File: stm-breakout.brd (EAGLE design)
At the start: 68 x 68 mm, 5 parts, among them IC1 STM32H757IIT6

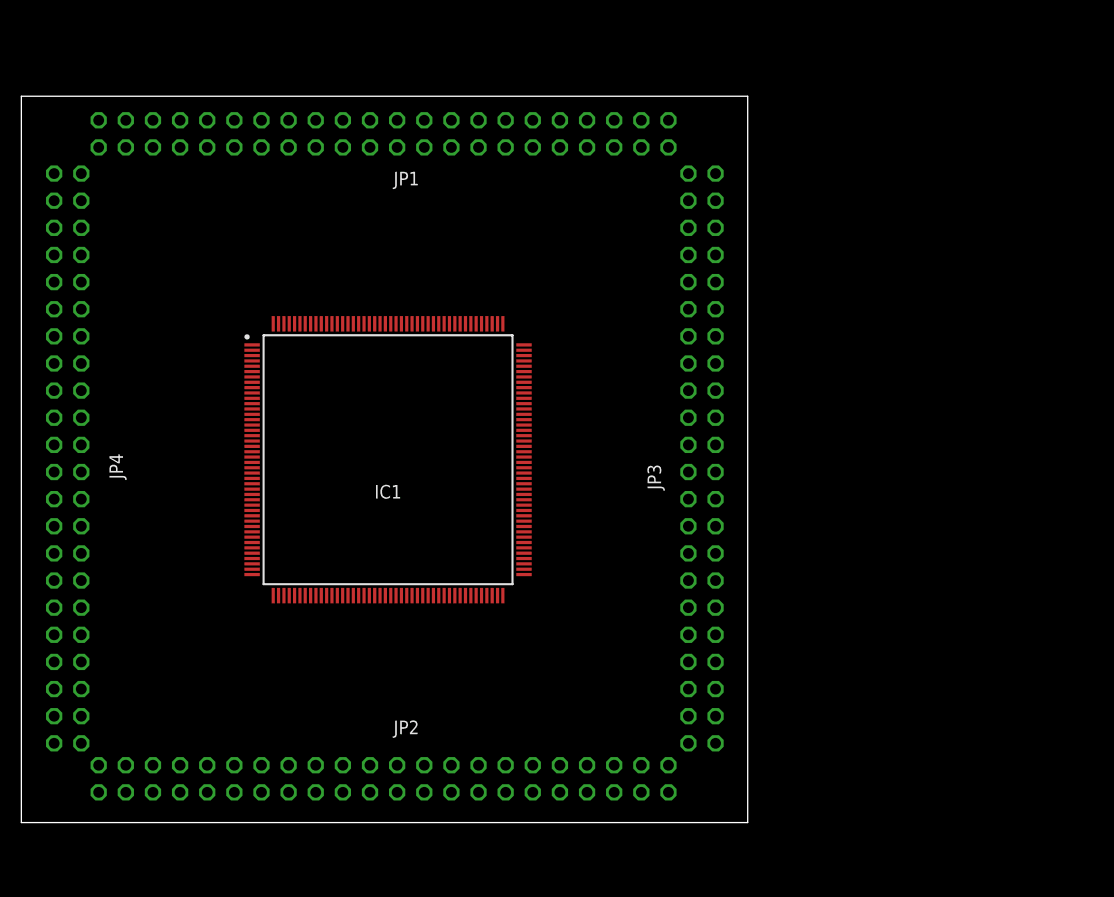
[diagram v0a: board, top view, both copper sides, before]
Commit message: Add in power filtering and SMPS functionality
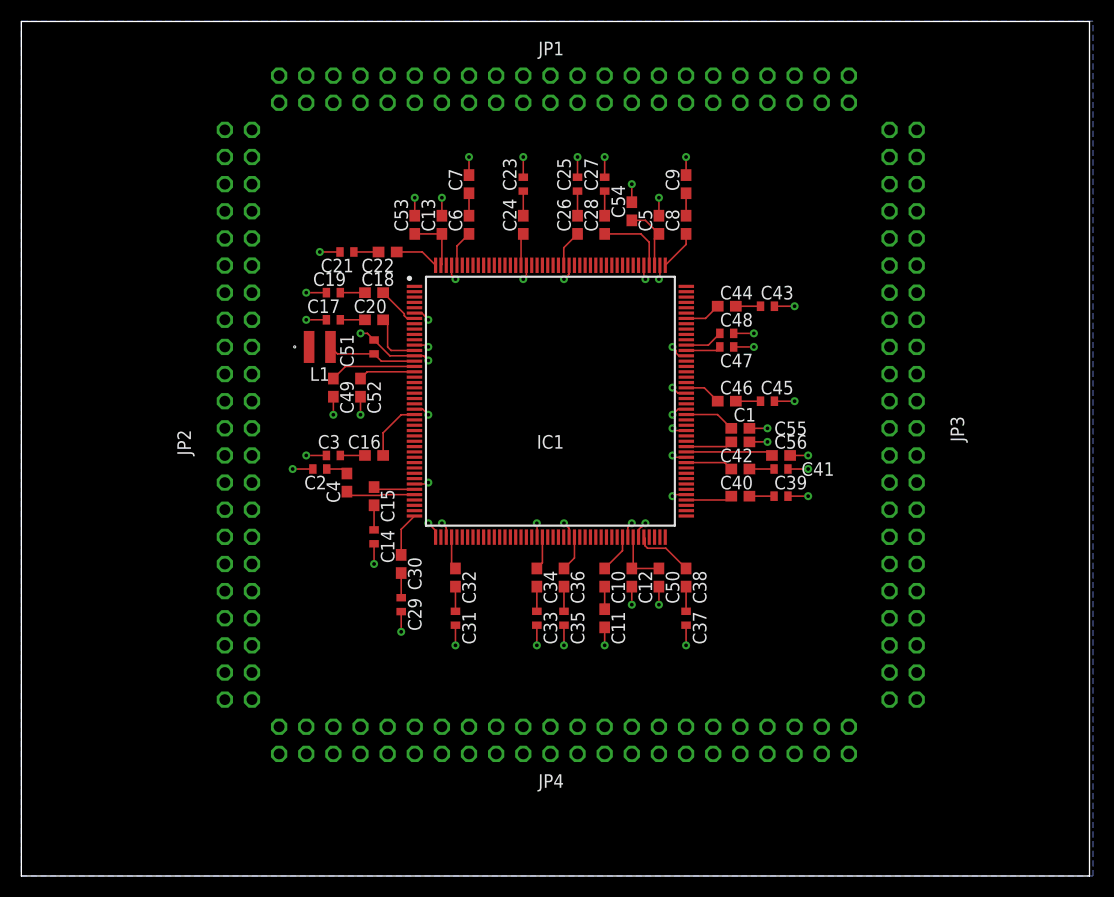
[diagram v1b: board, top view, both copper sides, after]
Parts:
- added C1, C10, C11, C55, C56, C6, C7, C8, C9: 2.2u, rcl:C0603
- added C12, C13, C16, C18, C20, C22, C24, C26, C28, C30, C32, C34, C36, C38, C40, C42, C44, C46, C49, C5: 4.7u, rcl:C0603
- added C14, C17, C19, C2, C21, C23, C25, C27, C29, C3, C31, C33, C35, C37, C39, C41, C43, C45, C47, C48: 100n, rcl:C0402
- added C15, C4: 1u, rcl:C0603
- added C50, C52, C53, C54: 10u, rcl:C0603
- added C51: 220p, rcl:C0402
- added L1: VLS3015CX-2R2M-H, SamacSys_Parts:VLS3015
- moved JP4 51.7 mm to (49.5, 12.7), turned to 180 degrees
- moved JP2 36.0 mm to (20.3, 41.9), turned to 90 degrees
- moved JP3 19.3 mm to (82.5, 41.9)
- moved IC1 16.2 mm to (49.5, 44.5)
- moved JP1 14.9 mm to (49.5, 73.7), turned to 180 degrees
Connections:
- new net GND: C1.2, C11.2, C12.2, C13.2, C14.2, C17.2, C19.2, C2.2, C21.2, C23.2, C25.2, C27.2, C29.2, C3.2, C31.2, C33.2, C35.2, C37.2, C39.2, C41.2, C43.2, C45.2, C47.2, C48.2, C49.2, C5.2, C50.2, C51.2, C52.2, C53.2, C54.2, C55.2, C56.2, C7.2, C9.2, IC1.100, IC1.105, IC1.109, IC1.112, IC1.119, IC1.12, IC1.134, IC1.137, IC1.14, IC1.151, IC1.159, IC1.173, IC1.24, IC1.38, IC1.45, IC1.47, IC1.6, IC1.64, IC1.70, IC1.81, IC1.83, IC1.93
- new net N$1: C2.1, C4.2
- new net N$2: C6.2, C7.1
- new net N$3: C8.2, C9.1
- new net N$4: C10.2, C11.1
- new net VCAPDSI: C1.1, C55.1, C56.1, IC1.101, IC1.102, IC1.108
- new net VDD: C10.1, C12.1, C13.1, C16.1, C18.1, C20.1, C22.1, C24.1, C26.1, C28.1, C30.1, C32.1, C34.1, C36.1, C38.1, C4.1, C40.1, C42.1, C44.1, C46.1, C5.1, C50.1, C52.1, C53.1, C54.1, C6.1, C8.1, IC1.113, IC1.126, IC1.13, IC1.133, IC1.135, IC1.136, IC1.152, IC1.160, IC1.17, IC1.172, IC1.175, IC1.176, IC1.25, IC1.40, IC1.44, IC1.48, IC1.65, IC1.7, IC1.71, IC1.80, IC1.82, IC1.84, IC1.92, IC1.99, L1.1
- new net VDD33USB: C48.1, IC1.121
- new net VDD50USB: C47.1, IC1.120
- new net VIN: C49.1, IC1.16
- new net VLXSMPS: C51.1, IC1.15, L1.2
- new net VREF: C15.1, IC1.39
- new net VREFNF: C14.1, C15.2
- new net VREFNF1: C16.2, C3.1
- new net VREFNF10: C33.1, C34.2
- new net VREFNF11: C35.1, C36.2
- new net VREFNF12: C37.1, C38.2
- new net VREFNF13: C39.1, C40.2
- new net VREFNF14: C41.1, C42.2
- new net VREFNF15: C43.1, C44.2
- new net VREFNF16: C45.1, C46.2
- new net VREFNF2: C17.1, C18.2
- new net VREFNF3: C19.1, C20.2
- new net VREFNF4: C21.1, C22.2
- new net VREFNF5: C23.1, C24.2
- new net VREFNF6: C25.1, C26.2
- new net VREFNF7: C27.1, C28.2
- new net VREFNF8: C29.1, C30.2
- new net VREFNF9: C31.1, C32.2
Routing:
- net VDD: track 0.00 -> 107.1 mm
- net GND: track 0.00 -> 99.5 mm, vias 0 -> 57
- net VCAPDSI: track 0.00 -> 17.3 mm
- net VLXSMPS: track 0.00 -> 8.42 mm
- net VIN: track 0.00 -> 8.06 mm
- net VREF: track 0.00 -> 3.87 mm
- net VDD33USB: track 0.00 -> 3.60 mm
- net VDD50USB: track 0.00 -> 3.27 mm
- net VREFNF7: track 0.00 -> 2.31 mm
- net VREFNF6: track 0.00 -> 2.31 mm
- net VREFNF5: track 0.00 -> 2.31 mm
- net VREFNF3: track 0.00 -> 2.31 mm
- net VREFNF2: track 0.00 -> 2.31 mm
- net VREFNF16: track 0.00 -> 2.31 mm
- net VREFNF15: track 0.00 -> 2.31 mm
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- added copper zone on layer 16, net GND
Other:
- board size 68 x 68 mm -> 100 x 80 mm

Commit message: Add nrst switch, sdcard, TFT display connector, and jtag
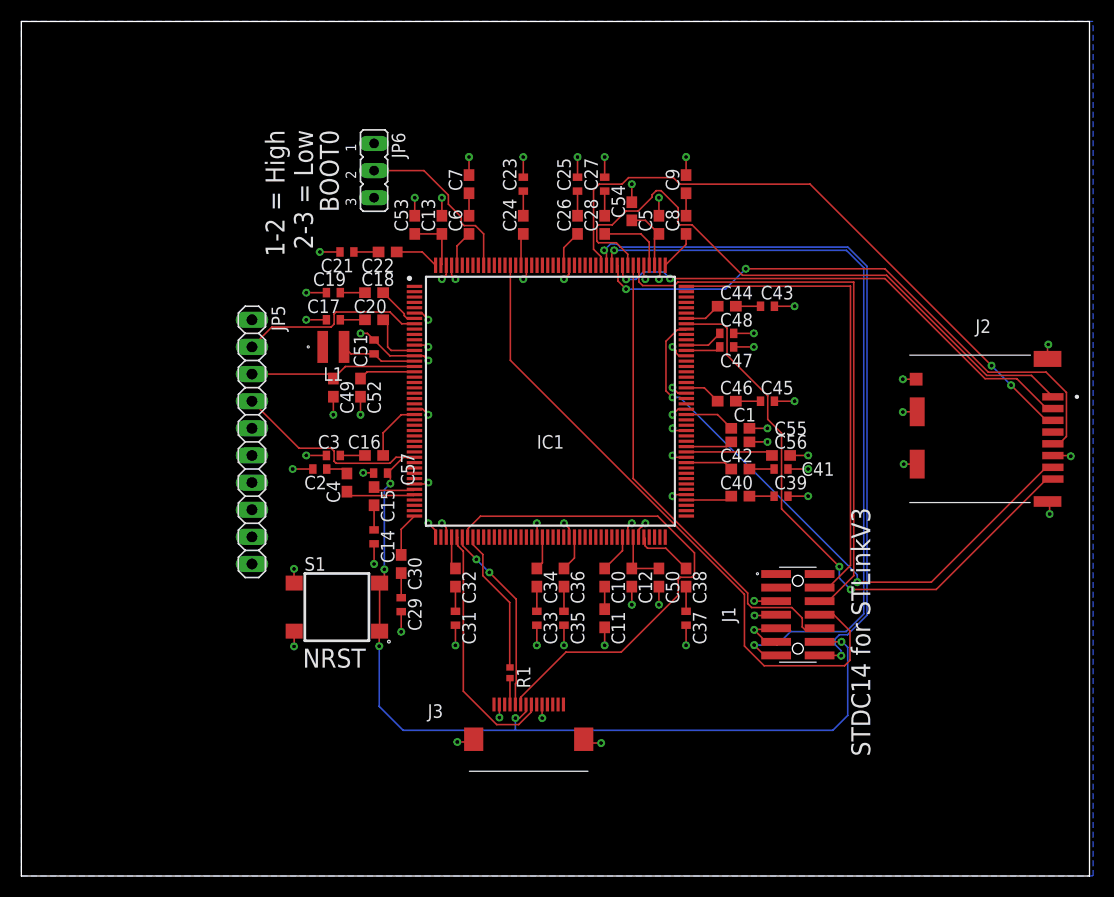
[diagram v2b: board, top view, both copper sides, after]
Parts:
- removed JP1, JP2, JP3, JP4: (no value), pinhead:2X22
- added C57: 100n, rcl:C0402
- added J1: FTSH-107-01-L-DV-K-A, SamacSys_Parts:FTSH-107-XX-YYY-DV-K-A
- added J2: DM3CS-SF, SamacSys_Parts:DM3CSSF
- added J3: FH12-14S-0.5SH_55_, SamacSys_Parts:FH1214S05SH55
- added JP5: (no value), pinhead:1X10
- added JP6: (no value), SamacSys_Parts:JP2
- added R1: 1k, rcl:R0402
- added S1: B3FS-1000P, SamacSys_Parts:B3FS-1000P
- moved L1 1.27 mm to (29.2, 49.5)
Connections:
- new net BOOT0: IC1.167, JP6.2
- new net DA: J3.11, R1.2
- new net JCLK: IC1.138, J1.6
- new net JTDI: IC1.139, J1.10
- new net JTDO: IC1.162, J1.8
- new net JTMS: IC1.132, J1.4
- new net NRST: C57.1, IC1.33, J1.12, J3.8, JP5.4, S1.1, S1.3
- new net RS: IC1.51, J3.9
- new net SDMMC1_CK: IC1.142, J2.5
- new net SDMMC1_CMD: IC1.145, J2.3
- new net SDMMC1_D0: IC1.124, J2.7
- new net SDMMC1_D1: IC1.125, J2.8
- new net SDMMC1_D2: IC1.140, J2.1
- new net SDMMC1_D3: IC1.141, J2.2
- new net SPI1_MOSI: IC1.52, R1.1
- new net SPI1_NSS: IC1.49, J3.7
- new net SPI1_SCK: IC1.50, J3.10
- new net UART4_RX: IC1.143, J1.13
- new net UART4_TX: IC1.144, J1.14
- new net VBAT: IC1.8, JP5.2
- new net XL: J3.2
- new net XR: J3.4
- new net YD: J3.3
- new net YU: J3.1
- net GND: now also C57.2, IC1.174, J1.11, J1.5, J1.7, J1.9, J2.6, J2.MP1, J2.MP2, J2.MP3, J2.MP4, J2.MP5, J3.13, J3.5, J3.MP1, J3.MP2, JP5.1, JP6.3, S1.2, S1.4
- net VDD: now also J1.3, J2.4, J3.14, J3.6, JP6.1
- net VIN: now also JP5.3
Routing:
- net NRST: track 0.00 -> 101.6 mm, vias 0 -> 5
- net UART4_RX: track 0.00 -> 71.9 mm, vias 0 -> 2
- net UART4_TX: track 0.00 -> 67.6 mm, vias 0 -> 2
- net JTDO: track 0.00 -> 61.8 mm
- net SDMMC1_CMD: track 0.00 -> 60.2 mm, vias 0 -> 2
- net SDMMC1_D2: track 0.00 -> 58.9 mm
- net SDMMC1_D1: track 0.00 -> 56.5 mm, vias 0 -> 2
- net SDMMC1_D0: track 0.00 -> 55.5 mm, vias 0 -> 2
- net SDMMC1_CK: track 0.00 -> 55.1 mm, vias 0 -> 2
- net JCLK: track 0.00 -> 53.6 mm
- net RS: track 0.00 -> 48.5 mm
- net SDMMC1_D3: track 0.00 -> 47.0 mm, vias 0 -> 2
- net JTMS: track 0.00 -> 45.3 mm
- net JTDI: track 0.00 -> 44.5 mm
- net GND: track 99.5 -> 127.6 mm, vias 57 -> 74
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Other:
- board text added: "1-2 = High 2-3 = Low"
- board text added: "BOOT0"
- board text added: "NRST"
- board text added: "STDC14 for STLinkV3"
